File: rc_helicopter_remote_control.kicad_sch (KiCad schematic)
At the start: 15 parts, among them J1 SWD, U1 STM32L4P5RET6, Y1 16MHz

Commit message: Improve DCDC converter diagram
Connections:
- net +3.3V: now also JOY1.1 (V+), JOY1.4 (H+), JOY2.1 (V+), JOY2.4 (H+); no longer JOY1.H1 (H+), JOY1.V1 (V+), JOY2.H1 (H+), JOY2.V1 (V+)
- net GND: now also JOY1.3 (V-), JOY1.6 (H-), JOY1.8 (SEL-), JOY1.9 (SHIELD), JOY2.3 (V-), JOY2.6 (H-), JOY2.8 (SEL-), JOY2.9 (SHIELD); no longer BT1.2 (-), JOY1.B2A (SEL-), JOY1.H3 (H-), JOY1.S1 (SHIELD), JOY1.S2 (SHIELD), JOY1.S3 (SHIELD), JOY1.S4 (SHIELD), JOY1.V3 (V-), JOY2.B2A (SEL-), JOY2.H3 (H-), JOY2.S1 (SHIELD), JOY2.S2 (SHIELD), JOY2.S3 (SHIELD), JOY2.S4 (SHIELD), JOY2.V3 (V-)
- net JOY1_S: now also JOY1.7 (SEL+), JOY2.7 (SEL+); no longer JOY1.B1A (SEL+)
- net JOY1_X: now also JOY1.5 (H), JOY2.5 (H); no longer JOY1.H2 (H)
- net JOY1_Y: now also JOY1.2 (V), JOY2.2 (V); no longer JOY1.V2 (V)
- net JOY2_S: no longer JOY2.B1A (SEL+)
- net JOY2_X: no longer JOY2.H2 (H)
- net JOY2_Y: no longer JOY2.V2 (V)
- net +BATT renamed Power/+BATT
- new net Power/GND: BT1.2 (-)
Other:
- moved on the sheet: BT1, C3, C4, C5, C6, C7, J1

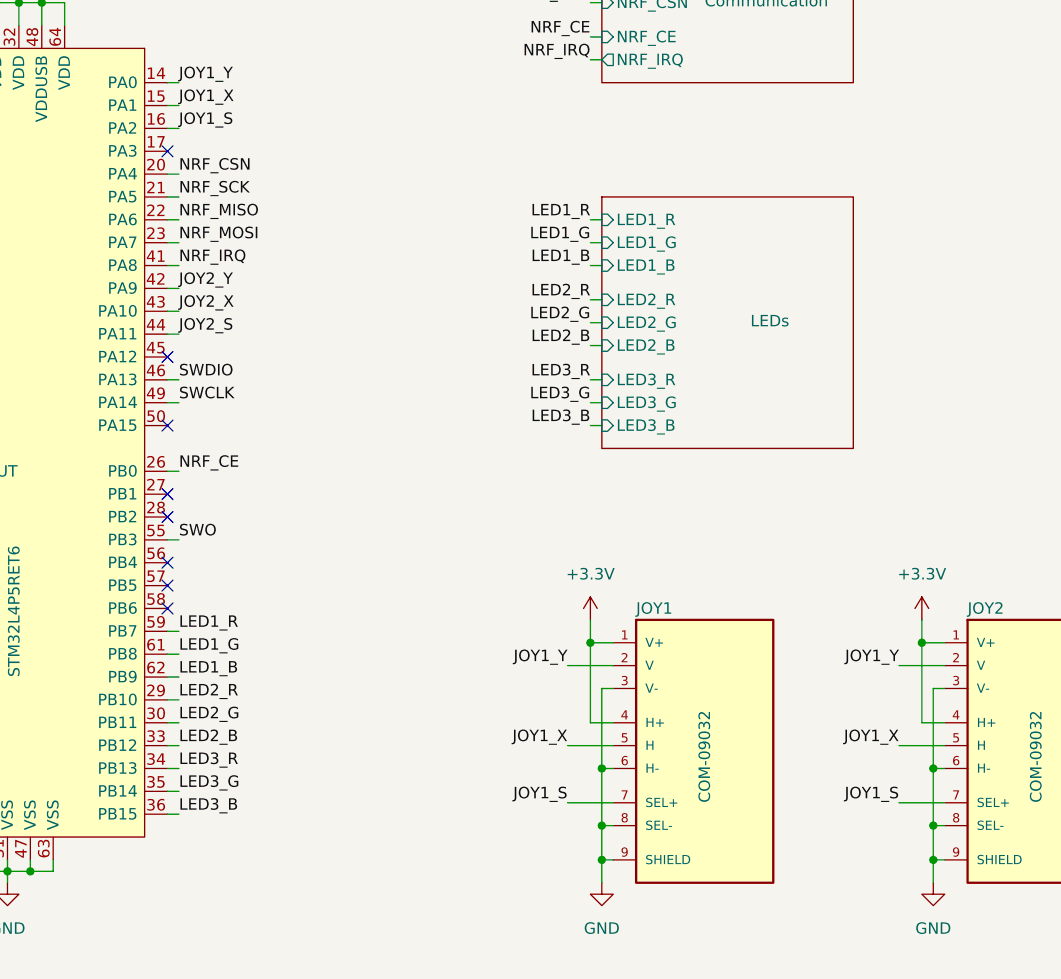
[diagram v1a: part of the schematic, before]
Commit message: Replace RGB leds with single color ones
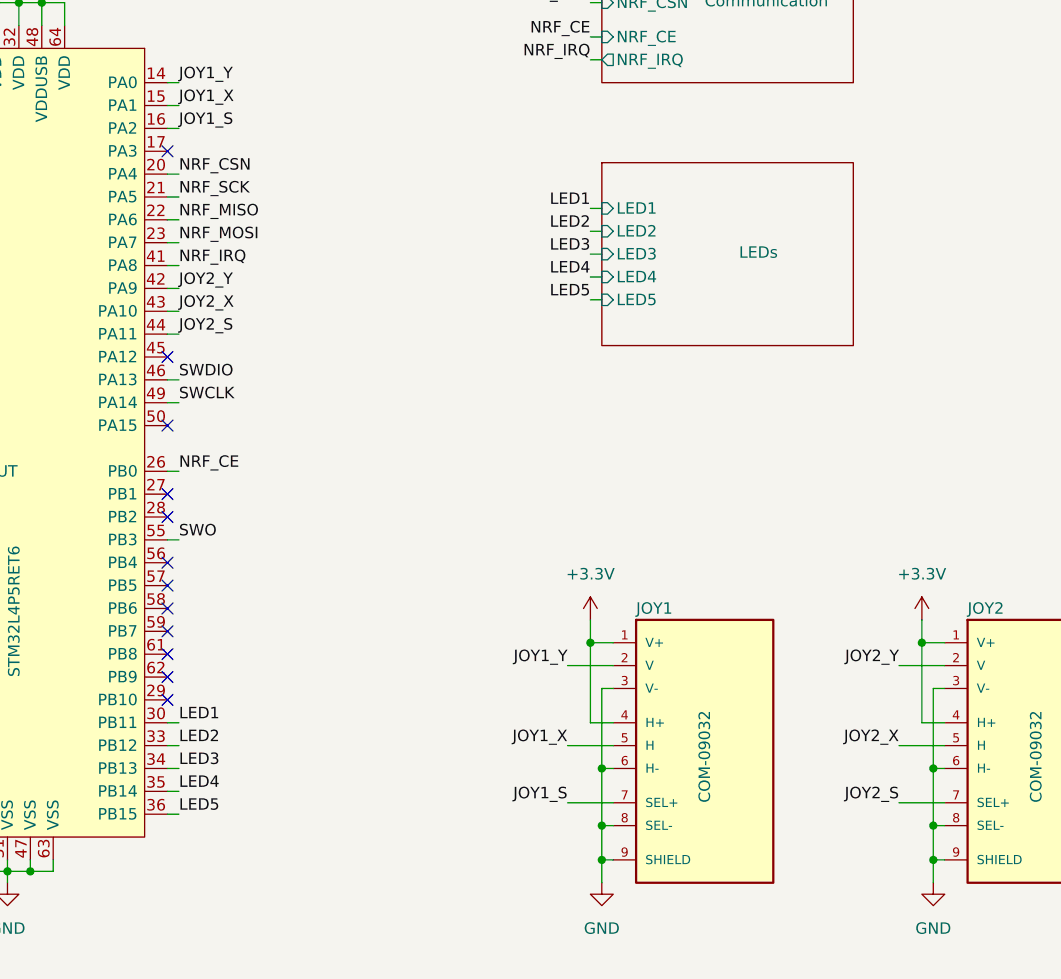
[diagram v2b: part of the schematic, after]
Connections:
- net JOY1_S: no longer JOY2.7 (SEL+)
- net JOY1_X: no longer JOY2.5 (H)
- net JOY1_Y: no longer JOY2.2 (V)
- net JOY2_S: now also JOY2.7 (SEL+)
- net JOY2_X: now also JOY2.5 (H)
- net JOY2_Y: now also JOY2.2 (V)
- net LED1_B: no longer names the net of U1.62 (PB9)
- net LED1_G: no longer names the net of U1.61 (PB8)
- net LED1_R: no longer names the net of U1.59 (PB7)
- net LED2_B renamed LED2
- net LED2_G renamed LED1
- net LED2_R: no longer names the net of U1.29 (PB10)
- net LED3_B renamed LED5
- net LED3_G renamed LED4
- net LED3_R renamed LED3
- no-connect marks 25 -> 29
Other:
- sheet LEDs ports: added LED1, LED2, LED3, LED4, LED5; removed LED1_B, LED1_G, LED1_R, LED2_B, LED2_G, LED2_R, LED3_B, LED3_G, LED3_R

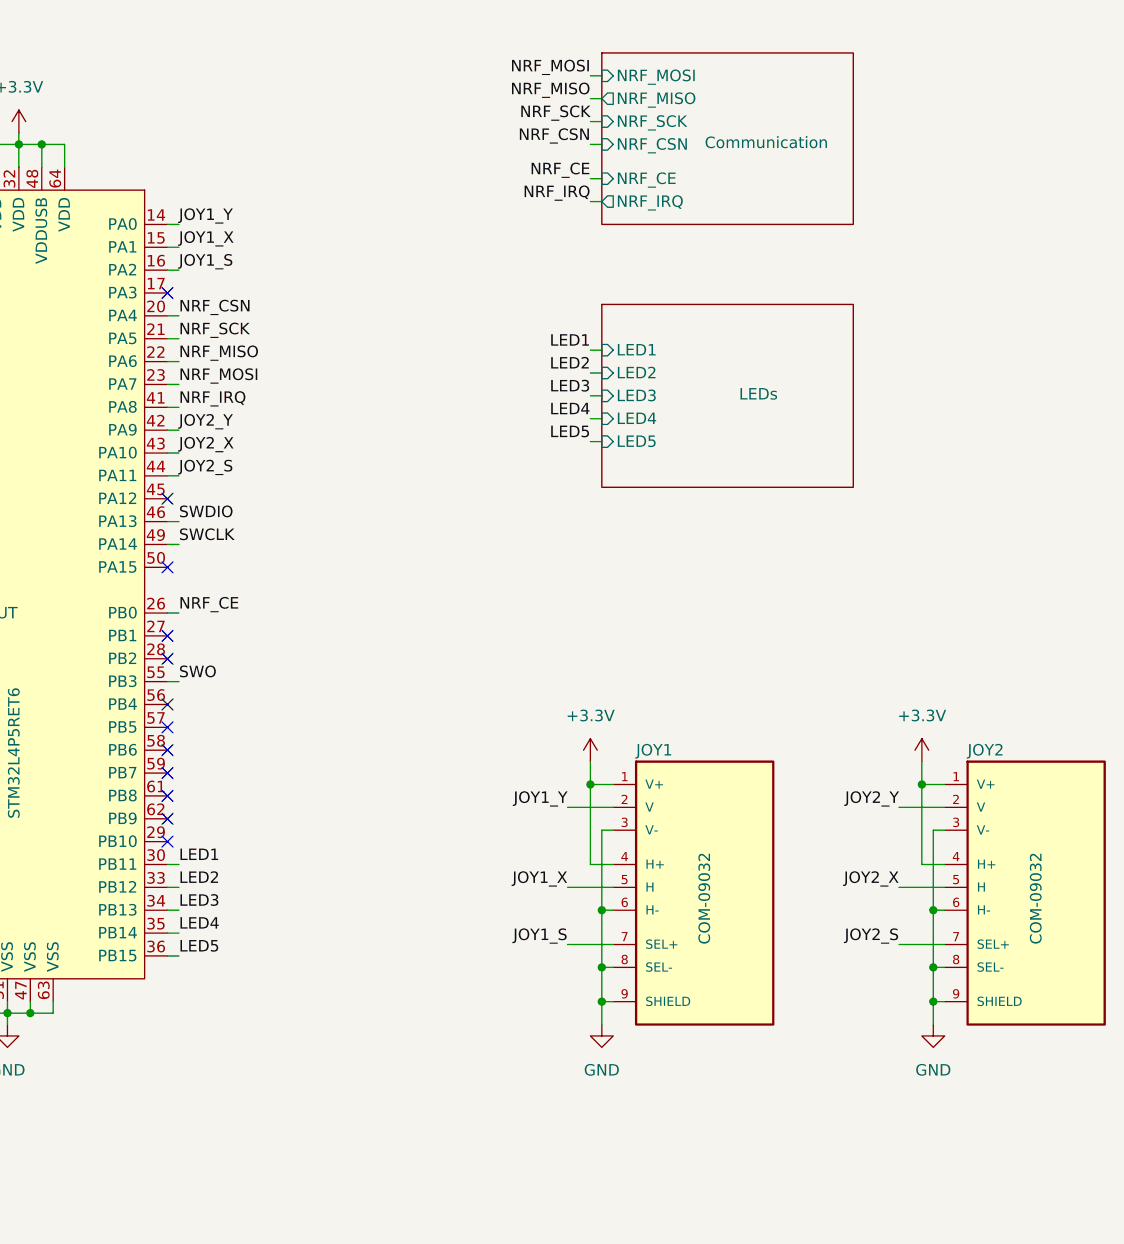
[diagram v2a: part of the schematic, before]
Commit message: Add buttons and trimmers
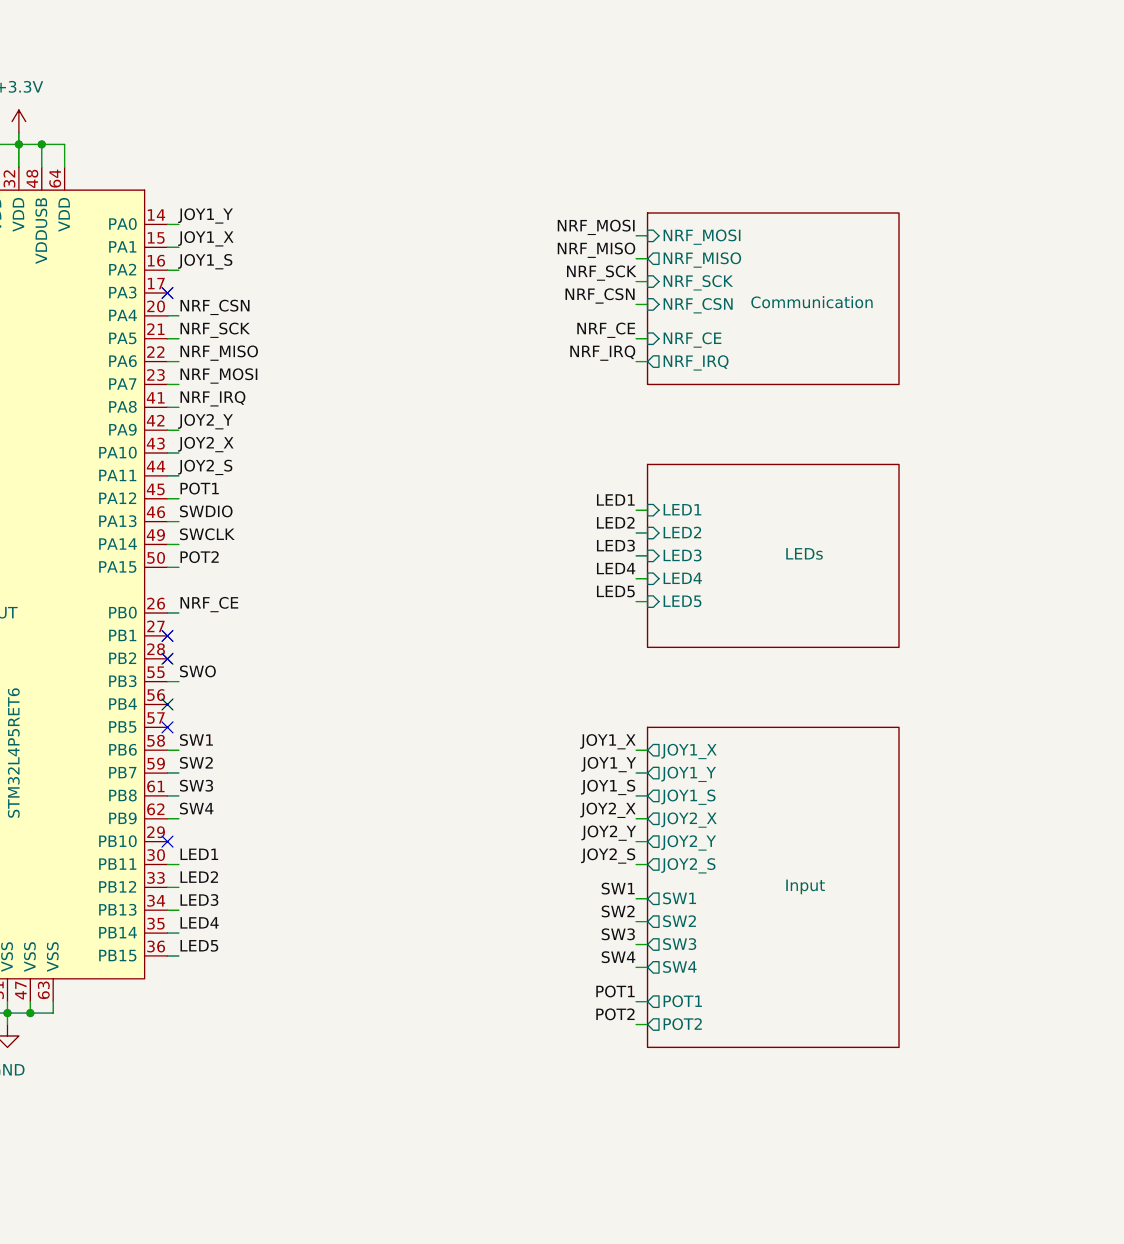
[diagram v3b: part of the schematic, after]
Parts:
- removed JOY1, JOY2: COM-09032, XDCR_COM-09032, symbol COM-09032:COM-09032
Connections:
- net POT1: now reaches U1.45 (PA12)
- net POT2: now reaches U1.50 (PA15)
- net SW1: now reaches U1.58 (PB6)
- net SW2: now reaches U1.59 (PB7)
- net SW3: now reaches U1.61 (PB8)
- net SW4: now reaches U1.62 (PB9)
- no-connect marks 29 -> 23
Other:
- added sheet Input (input.kicad_sch)

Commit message: Arrange footprints
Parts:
- removed BT1: Li-Ion, Local_Library:BAT_BCAAAW, symbol Device:Battery_Cell
- added J1: Battery Pack, Connector_Molex:Molex_KK-254_AE-6410-02A_1x02_P2.54mm_Vertical, symbol Connector_Generic:Conn_01x02
- J2: renamed from J1; footprint Connector_PinHeader_2.54mm:PinHeader_2x03_P2.54mm_Vertical -> Connector_PinHeader_2.54mm:PinHeader_1x06_P2.54mm_Vertical_SMD_Pin1Left
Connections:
- net GND: now also J1.2 (Pin_2)
- new net +BATT: J1.1 (Pin_1)
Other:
- note added: "+"
- note added: "-"
- note added: "Li-Ion Battery"
- note removed: "Battery Cell"
- moved on the sheet: J2

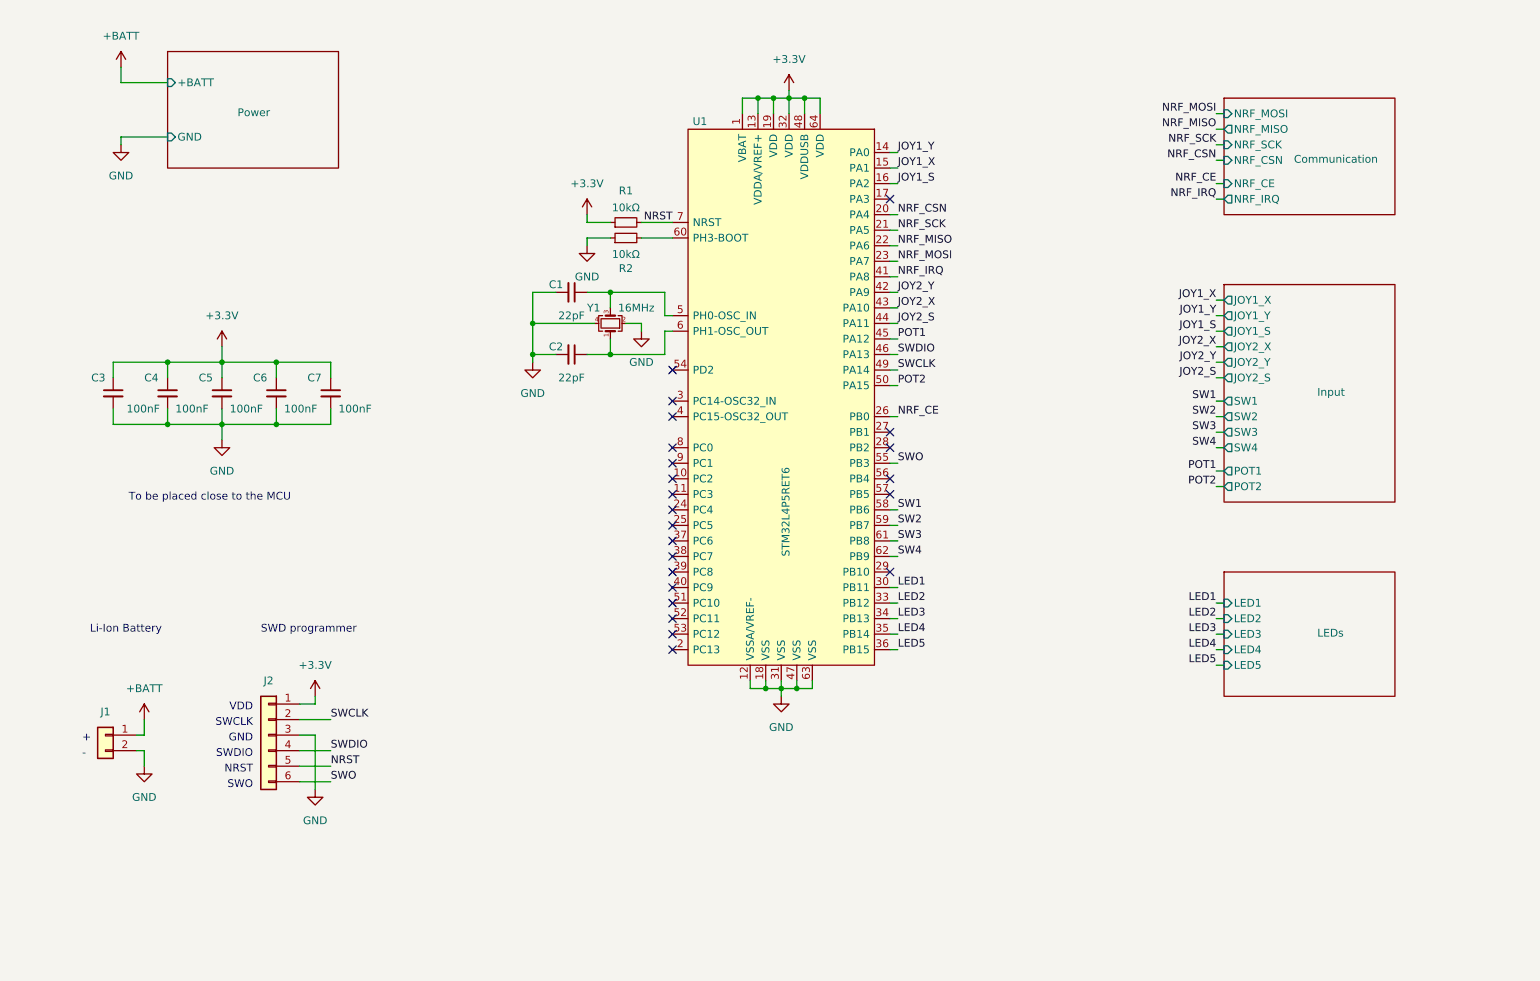
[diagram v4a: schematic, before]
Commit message: Use more appropriate MCU pins for peripherals
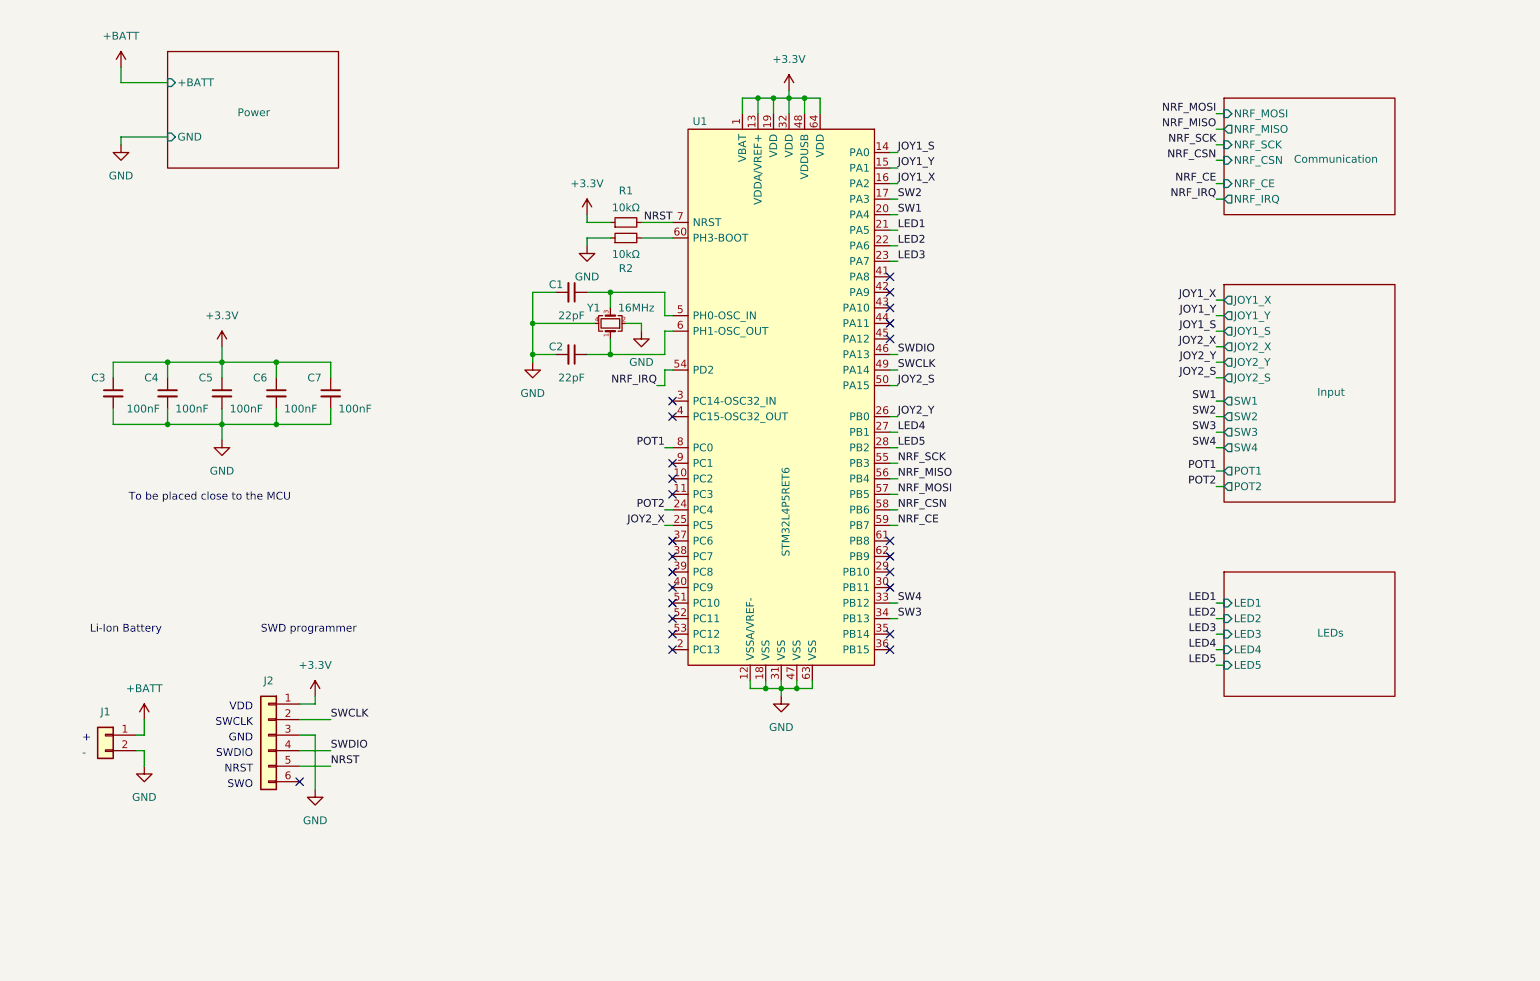
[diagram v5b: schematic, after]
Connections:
- net JOY1_S: now also U1.14 (PA0); no longer U1.16 (PA2)
- net JOY1_X: now also U1.16 (PA2); no longer U1.15 (PA1)
- net JOY1_Y: now also U1.15 (PA1); no longer U1.14 (PA0)
- net JOY2_S: now also U1.50 (PA15); no longer U1.44 (PA11)
- net JOY2_X: now also U1.25 (PC5); no longer U1.43 (PA10)
- net JOY2_Y: now also U1.26 (PB0); no longer U1.42 (PA9)
- net LED1: now also U1.21 (PA5); no longer U1.30 (PB11)
- net LED2: now also U1.22 (PA6); no longer U1.33 (PB12)
- net LED3: now also U1.23 (PA7); no longer U1.34 (PB13)
- net LED4: now also U1.27 (PB1); no longer U1.35 (PB14)
- net LED5: now also U1.28 (PB2); no longer U1.36 (PB15)
- net NRF_CE: now also U1.59 (PB7); no longer U1.26 (PB0)
- net NRF_CSN: now also U1.58 (PB6); no longer U1.20 (PA4)
- net NRF_IRQ: now also U1.54 (PD2); no longer U1.41 (PA8)
- net NRF_MISO: now also U1.56 (PB4); no longer U1.22 (PA6)
- net NRF_MOSI: now also U1.57 (PB5); no longer U1.23 (PA7)
- net NRF_SCK: now also U1.55 (PB3); no longer U1.21 (PA5)
- net POT1: now also U1.8 (PC0); no longer U1.45 (PA12)
- net POT2: now also U1.24 (PC4); no longer U1.50 (PA15)
- net SW1: now also U1.20 (PA4); no longer U1.58 (PB6)
- net SW2: now also U1.17 (PA3); no longer U1.59 (PB7)
- net SW3: now also U1.34 (PB13); no longer U1.61 (PB8)
- net SW4: now also U1.33 (PB12); no longer U1.62 (PB9)
- net SWO: no longer names the net of J2.6 (Pin_6)
- net SWO: no longer U1.55 (PB3)
- no-connect marks 23 -> 25
